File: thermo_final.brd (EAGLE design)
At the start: 67.8 x 100.6 mm, 113 parts

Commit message: Feeling good, she better work
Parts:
- moved JP2 11.9 mm to (22.5, 81.3)
- moved JP1 9.17 mm to (19.8, 81.3)
- moved R36 6.29 mm to (19.8, 79.3), turned to 270 degrees
- moved R39 6.29 mm to (22.5, 79.3), turned to 90 degrees
- moved D2 3.54 mm to (30.0, 82.6)
- moved D1 2.67 mm to (14.5, 82.5)
- moved D20 1.12 mm to (27.4, 86.2)
- moved R38 1.11 mm to (25.8, 80.6)
- moved D3 0.92 mm to (19.5, 86.1)
- moved R37 0.78 mm to (16.6, 80.5)
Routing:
- net SCK: track 67.3 -> 82.4 mm
- net T3+: track 71.0 -> 83.6 mm, vias 3 -> 2
- net IPOUT: track 8.29 -> 2.17 mm
- net IMOUT: track 7.52 -> 2.23 mm
- net VDD: track 32.0 -> 36.3 mm, vias 1 -> 0
- net N$40: track 13.2 -> 11.4 mm
- net MISO: track 67.0 -> 68.5 mm

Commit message: Uploaded all necessary 3D models
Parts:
- C1, C2, C5, C6, C7: device SamacSys_Parts:CAPC1608X90N@1 -> SamacSys_Parts:CAPC1608X90N
- CONNECTOR_0, CONNECTOR_1, CONNECTOR_2, CONNECTOR_3, CONNECTOR_4, CONNECTOR_5, CONNECTOR_6, CONNECTOR_7: device PCC-SMD-20:OMEGA_PCC-SMD-20 -> SamacSys_Parts:OMEGA_PCC-SMD-20
- R3: device TNPW0402100RBYEP:RESC1005X40N -> SamacSys_Parts:RESC1005X40N

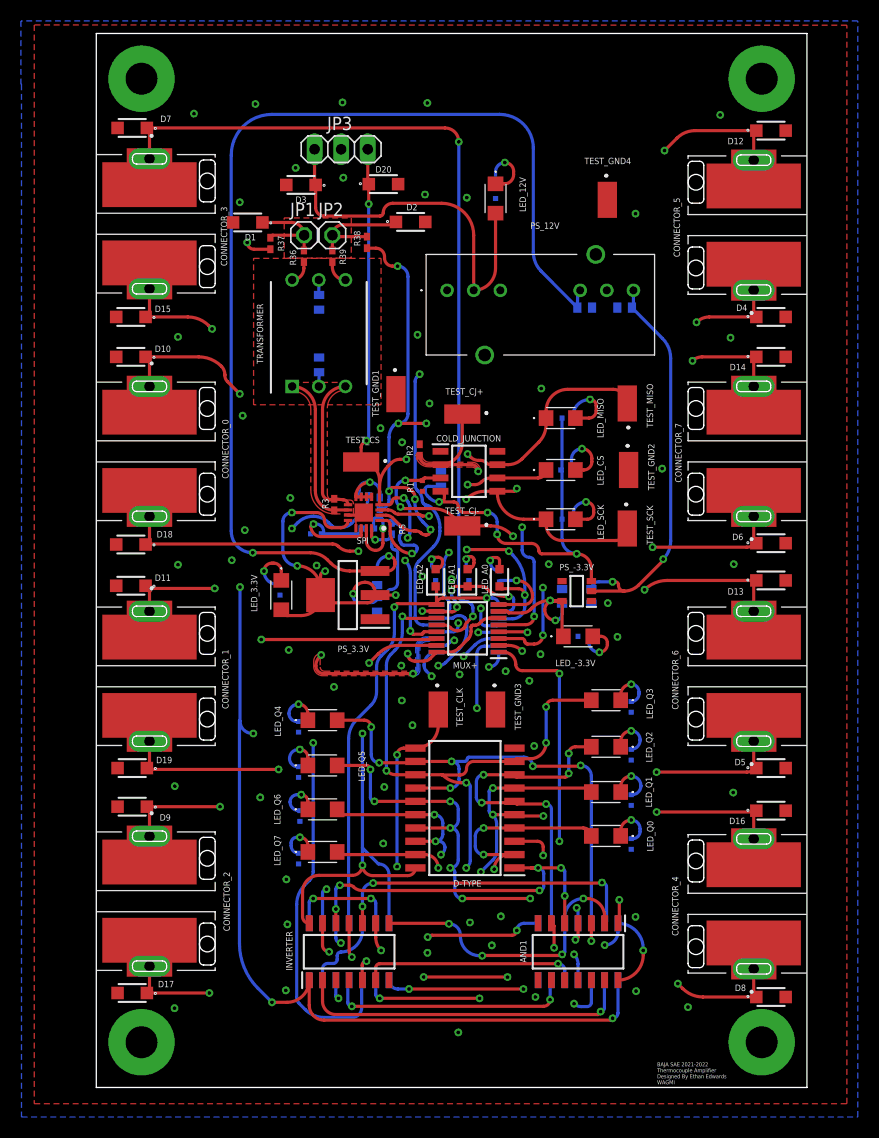
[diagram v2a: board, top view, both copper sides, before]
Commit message: Fixed Flip-Flop Footprint/Pushed 3D Model
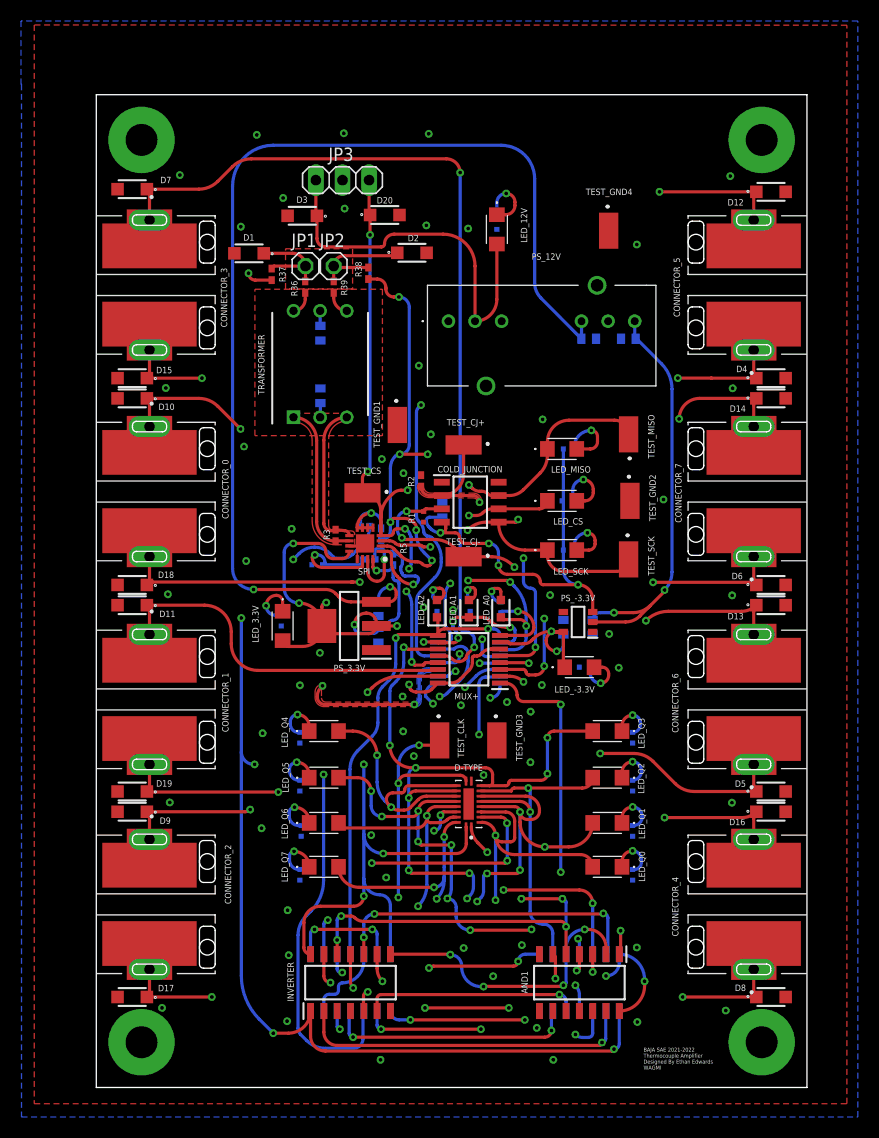
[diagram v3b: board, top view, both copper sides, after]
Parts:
- D-TYPE: device SamacSys_Parts:SOIC127P1032X265-20N -> SamacSys_Parts:QFN50P450X250X100-21N
- moved D15 5.84 mm to (3.43, 67.7)
- moved CONNECTOR_3 5.84 mm to (5.08, 76.6)
- moved D12 5.84 mm to (64.4, 85.5)
- moved D4 5.84 mm to (64.4, 67.7)
- moved D7 5.84 mm to (3.43, 85.7)
- moved U$1 5.84 mm to (4.32, 90.4)
- moved U$4 5.84 mm to (63.5, 90.4)
- moved CONNECTOR_5 5.72 mm to (62.7, 76.6)
- moved D6 3.99 mm to (64.4, 48.0)
- moved D10 3.96 mm to (3.43, 65.8)
- moved D14 3.96 mm to (64.4, 65.8)
- moved D18 3.86 mm to (3.43, 48.0)
- moved CONNECTOR_0 3.84 mm to (5.08, 56.9)
- moved CONNECTOR_7 3.84 mm to (62.7, 56.9)
- moved C3 3.00 mm to (47.0, 71.5)
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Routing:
- net Q1: track 53.2 -> 63.5 mm, vias 6 -> 7
- net Q3: track 92.4 -> 102.0 mm, vias 10 -> 13
- net Q7: track 26.7 -> 35.4 mm, vias 2 -> 4
- net CLK: track 43.4 -> 50.9 mm, vias 3 -> 4
- net !Q7: track 36.1 -> 43.4 mm
- net VCC: track 245.5 -> 252.3 mm, vias 19 -> 20
- net Q0: track 33.0 -> 39.7 mm, vias 4 -> 3
- net Q5: track 58.2 -> 64.6 mm, vias 9 -> 12
- net Q6: track 31.5 -> 36.3 mm, vias 4 -> 3
- net Q4: track 49.1 -> 52.6 mm, vias 6 -> 4
- net CS: track 199.2 -> 196.8 mm, vias 11 -> 13
- net T3-: track 54.4 -> 52.0 mm
- net T2-: track 54.1 -> 52.1 mm
- net V-: track 39.0 -> 41.1 mm
- net T4+: track 51.2 -> 49.3 mm
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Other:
- board size 67.8 x 100.6 mm -> 67.8 x 94.7 mm

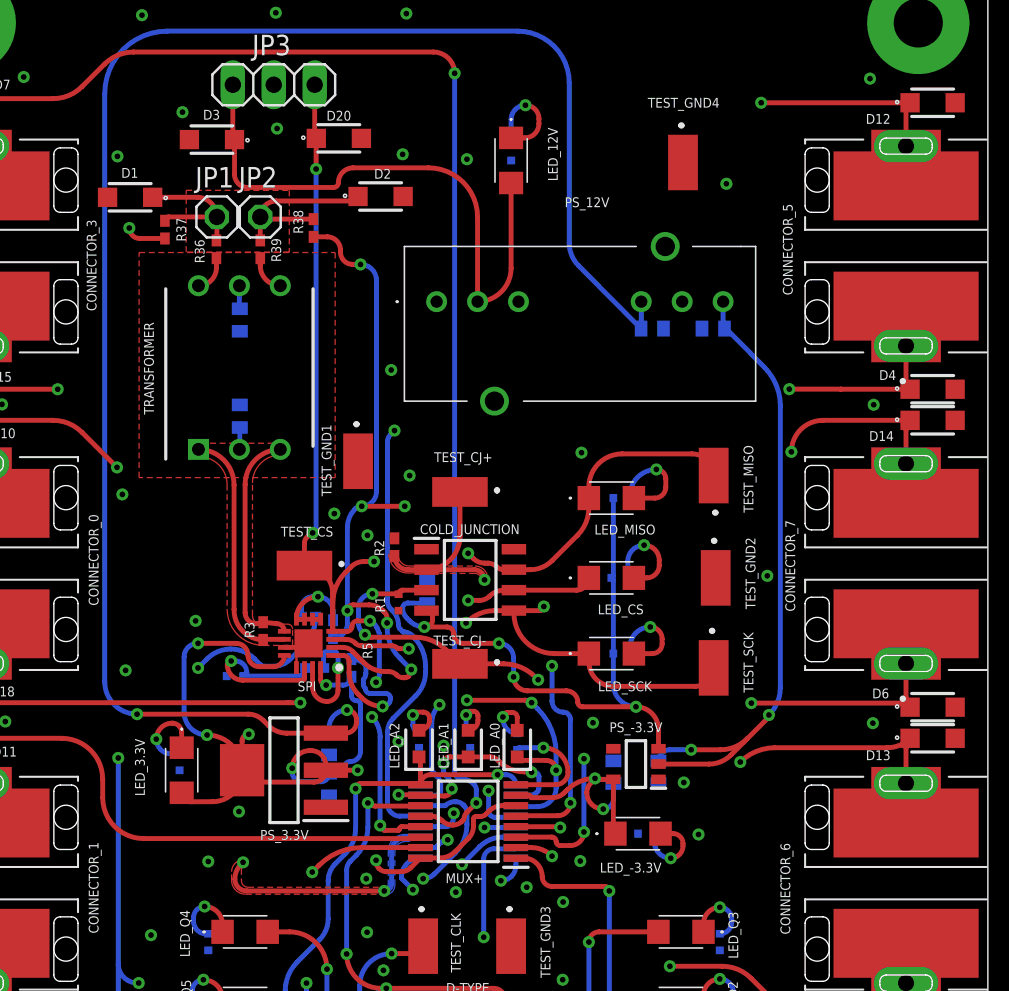
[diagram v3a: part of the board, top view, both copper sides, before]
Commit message: Added CMRR Caps at CJ input (Finalized)
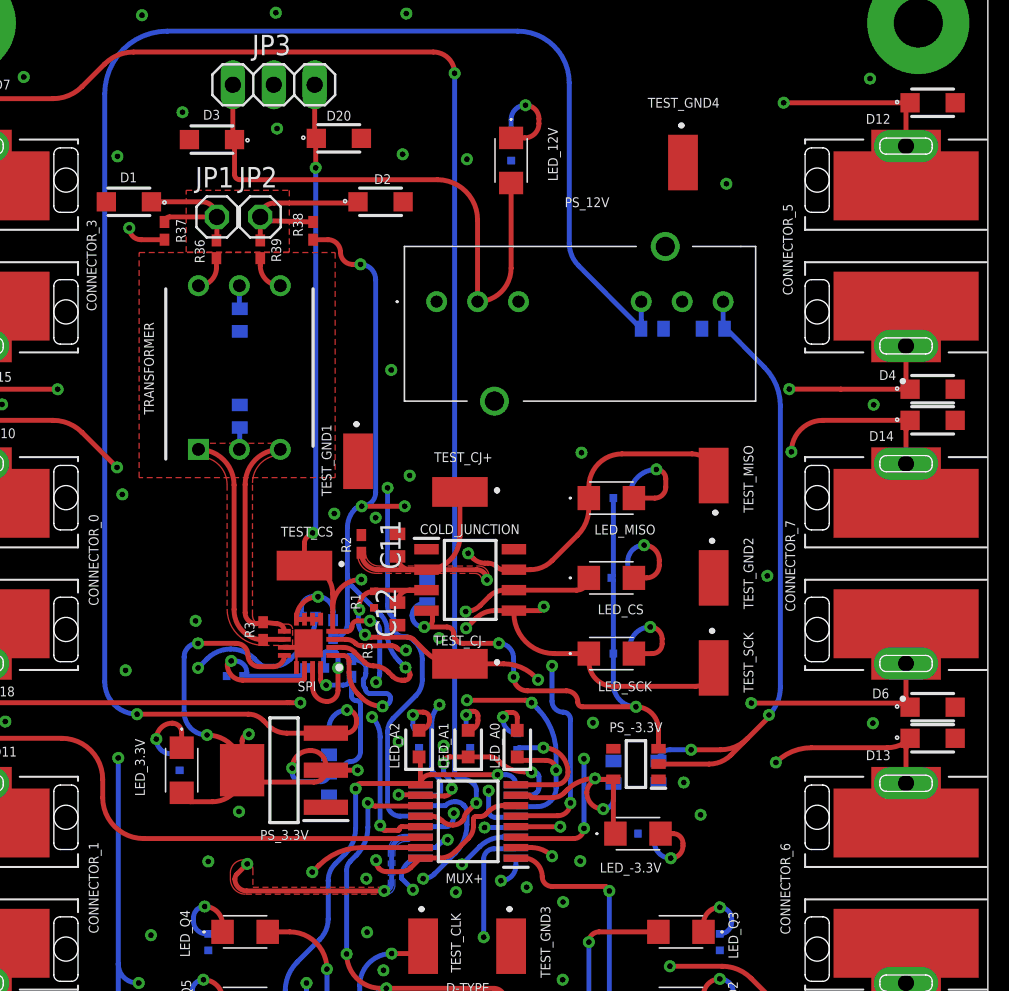
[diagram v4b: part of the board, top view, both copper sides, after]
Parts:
- added C11, C12: 06035C270JAT2A, SamacSys_Parts:CAPC1608X90N
- moved R2 2.07 mm to (28.9, 58.1)
- moved R1 1.53 mm to (29.7, 54.6)
- moved D2 0.33 mm to (30.1, 79.3)
- moved D1 0.29 mm to (14.5, 79.3)
- moved R38 0.18 mm to (25.9, 77.5)
- moved TEST_GND2 0.13 mm to (50.8, 56.0)
- moved R37 0.08 mm to (16.7, 77.5)
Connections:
- net CJ+: now also C12.1
- net CJ-: now also C11.2
- net GND: now also C11.1, C12.2
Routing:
- net CJ-: track 51.0 -> 55.6 mm
- net CS: track 196.8 -> 194.6 mm
- net CJ+: track 33.2 -> 34.9 mm
- net T5-: track 70.2 -> 68.8 mm
- net VDD: track 36.3 -> 35.2 mm
- net T0+: track 48.2 -> 47.3 mm
- net VCC: track 252.3 -> 251.4 mm
- net MISO: track 68.5 -> 69.0 mm, vias 7 -> 5
- net GND: vias 59 -> 60

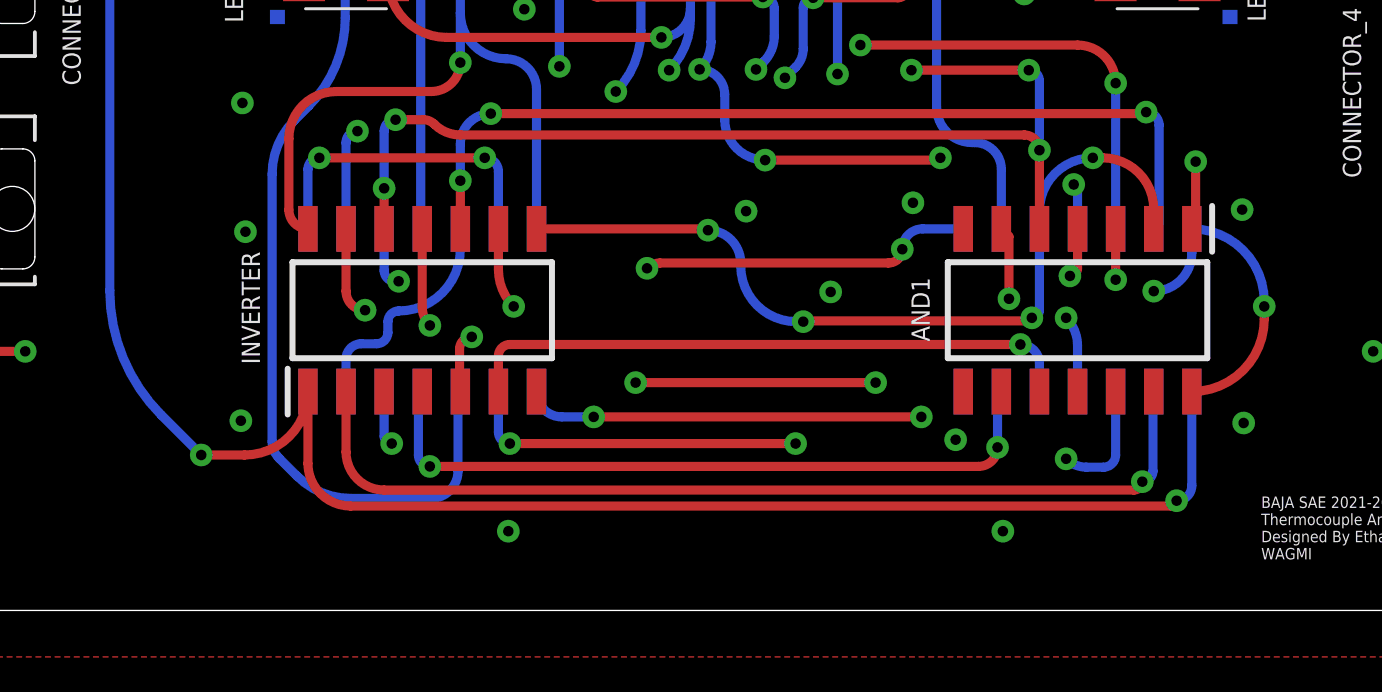
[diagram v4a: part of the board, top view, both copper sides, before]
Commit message: Final board/3d model with delay trigger fix
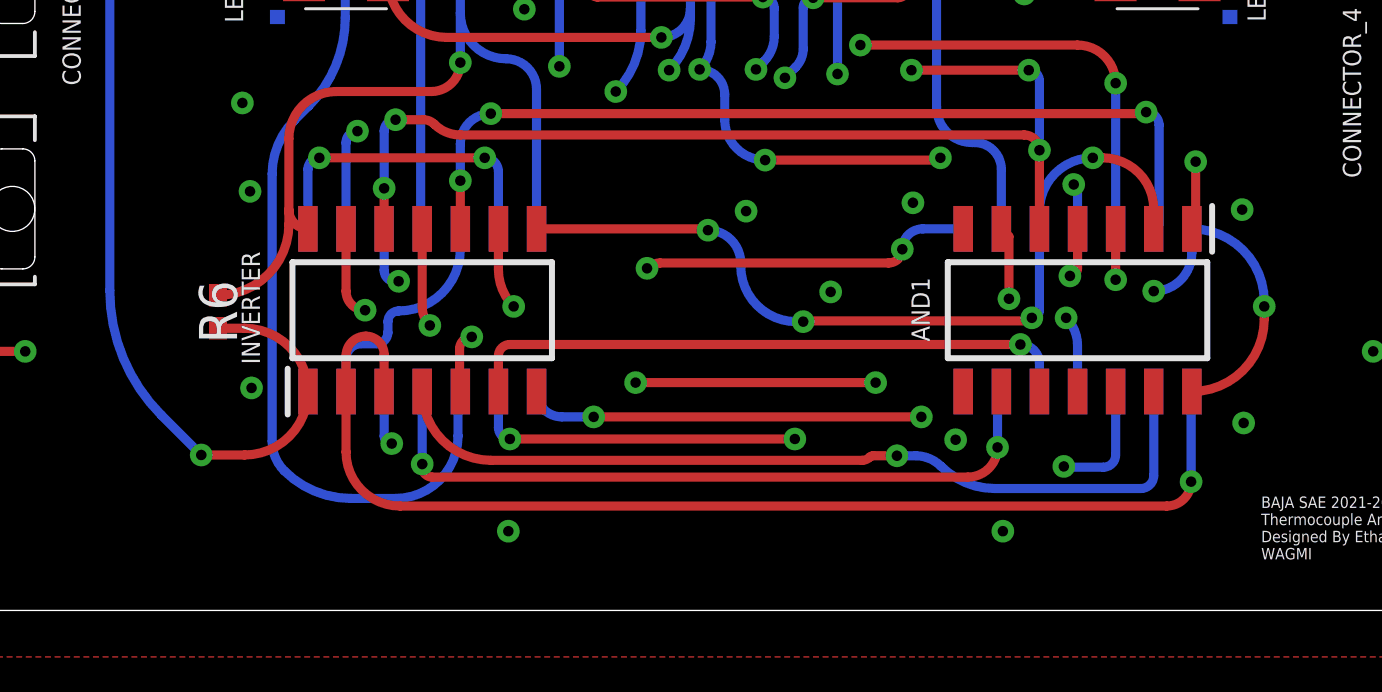
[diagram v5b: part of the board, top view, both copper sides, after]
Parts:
- added R6: RC0402FR-0793K1L, SamacSys_Parts:RESC1005X40N
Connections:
- new net !CS2: AND2.2, INVERTER.4
- net !CS: now also AND2.1, INVERTER.3; no longer AND2.2
- net CS: now also R6.2; no longer AND2.1
- net GND: no longer INVERTER.3, INVERTER.4
- net VCC: now also R6.1
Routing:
- net CS: track 194.6 -> 162.6 mm, vias 13 -> 12
- net !CS2: track 0.00 -> 28.6 mm, vias 0 -> 1
- net !CS: track 32.4 -> 38.5 mm
- net VCC: track 251.4 -> 255.2 mm
- net A1: track 65.2 -> 64.5 mm
